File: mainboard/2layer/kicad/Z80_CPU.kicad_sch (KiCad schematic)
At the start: 62 parts, among them J2 C96ABC, J9 DIN-5, U71 CDB407, U72 CDB407, U73 CDB407, U74 CDB407, U90 Z80CPU

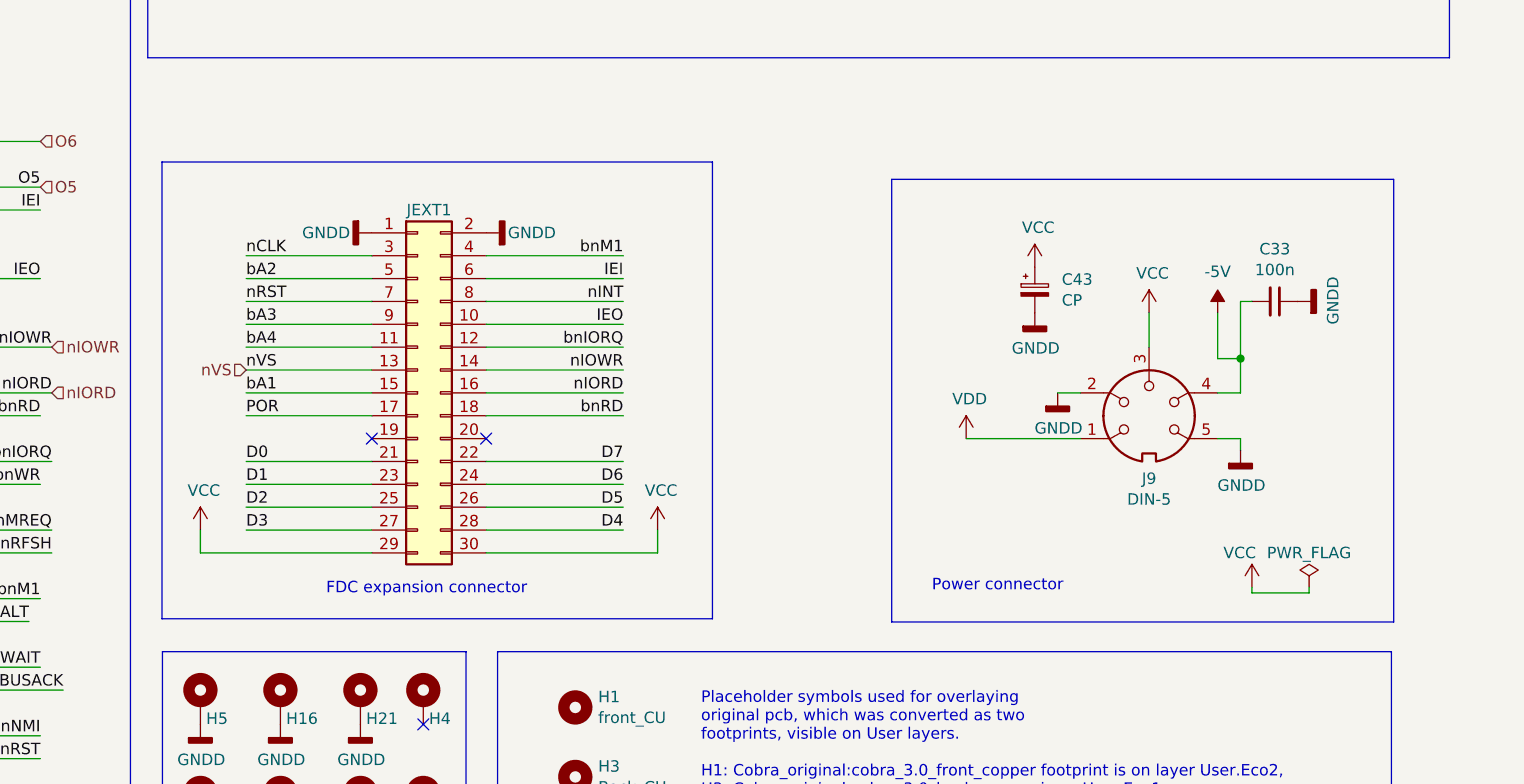
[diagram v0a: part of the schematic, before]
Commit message: Changed floppy connector, fixed some library paths
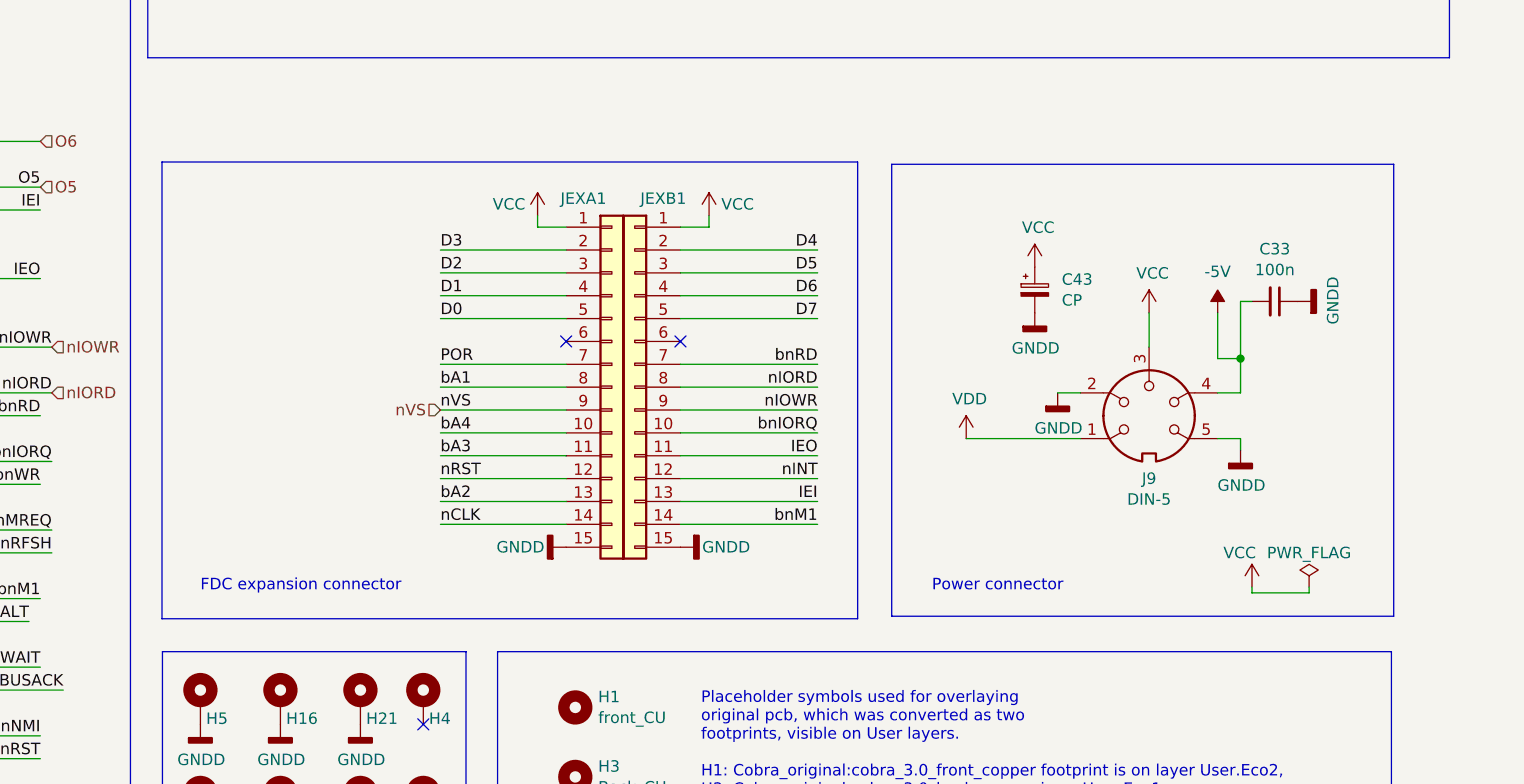
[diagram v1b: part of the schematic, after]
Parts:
- removed JEXT1: Conn_02x15_Odd_Even, Connector_PinHeader_2.54mm:PinHeader_2x15_P2.54mm_Vertical, symbol Connector_Generic:Conn_02x15_Odd_Even
- added JEXA1, JEXB1: Conn_01x15, Connector_PinHeader_2.54mm:PinHeader_1x15_P2.54mm_Vertical, symbol Connector_Generic:Conn_01x15
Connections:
- net D0: now also JEXA1.5 (Pin_5)
- net D1: now also JEXA1.4 (Pin_4)
- net D2: now also JEXA1.3 (Pin_3)
- net D3: now also JEXA1.2 (Pin_2)
- net D4: now also JEXB1.2 (Pin_2)
- net D5: now also JEXB1.3 (Pin_3)
- net D6: now also JEXB1.4 (Pin_4)
- net D7: now also JEXB1.5 (Pin_5)
- net GNDD: now also JEXA1.15 (Pin_15), JEXB1.15 (Pin_15)
- net IEI: now also JEXB1.13 (Pin_13)
- net IEO: now also JEXB1.11 (Pin_11)
- net POR: now also JEXA1.7 (Pin_7)
- net VCC: now also JEXA1.1 (Pin_1), JEXB1.1 (Pin_1)
- net bA1: now also JEXA1.8 (Pin_8)
- net bA2: now also JEXA1.13 (Pin_13)
- net bA3: now also JEXA1.11 (Pin_11)
- net bA4: now also JEXA1.10 (Pin_10)
- net bnIORQ: now also JEXB1.10 (Pin_10)
- net bnM1: now also JEXB1.14 (Pin_14)
- net bnRD: now also JEXB1.7 (Pin_7)
- net nCLK: now also JEXA1.14 (Pin_14)
- net nINT: now also JEXB1.12 (Pin_12)
- net nIORD: now also JEXB1.8 (Pin_8)
- net nIOWR: now also JEXB1.9 (Pin_9)
- net nRST: now also JEXA1.12 (Pin_12)
- net nVS: now also JEXA1.9 (Pin_9)

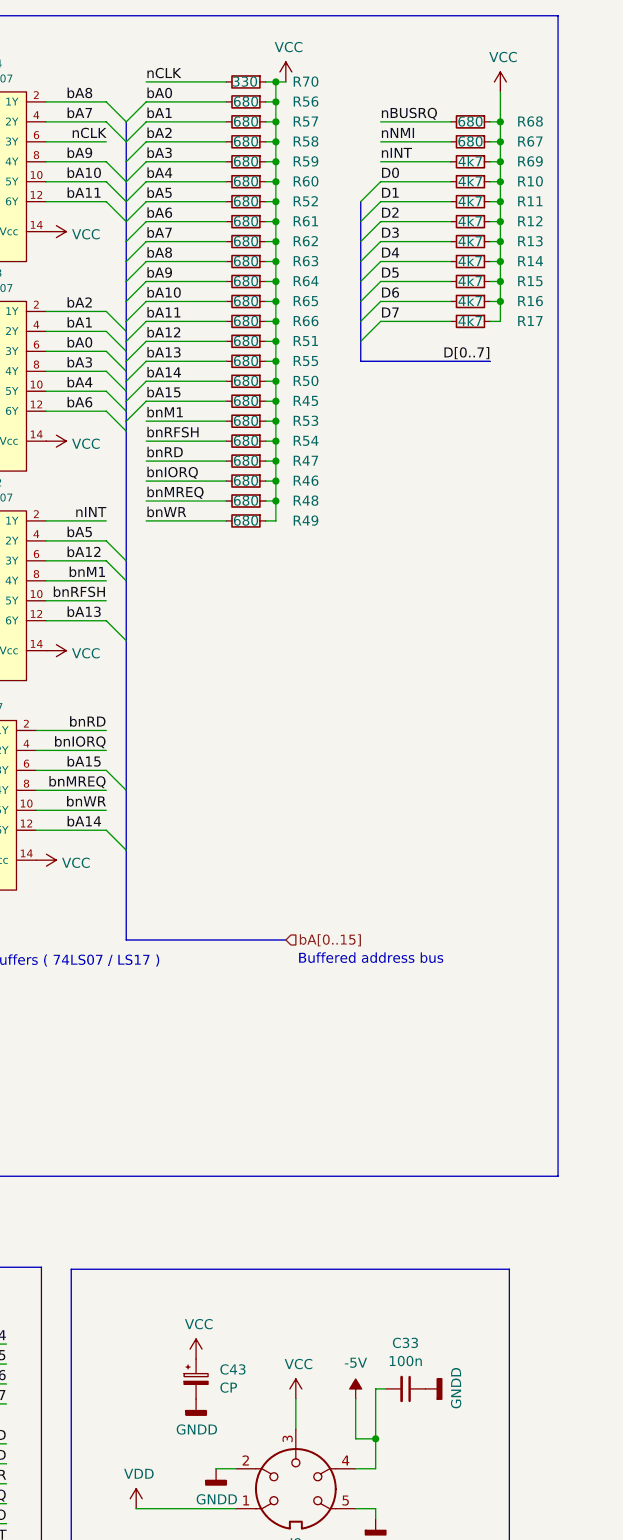
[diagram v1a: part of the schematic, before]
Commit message: Fixed some resistor values
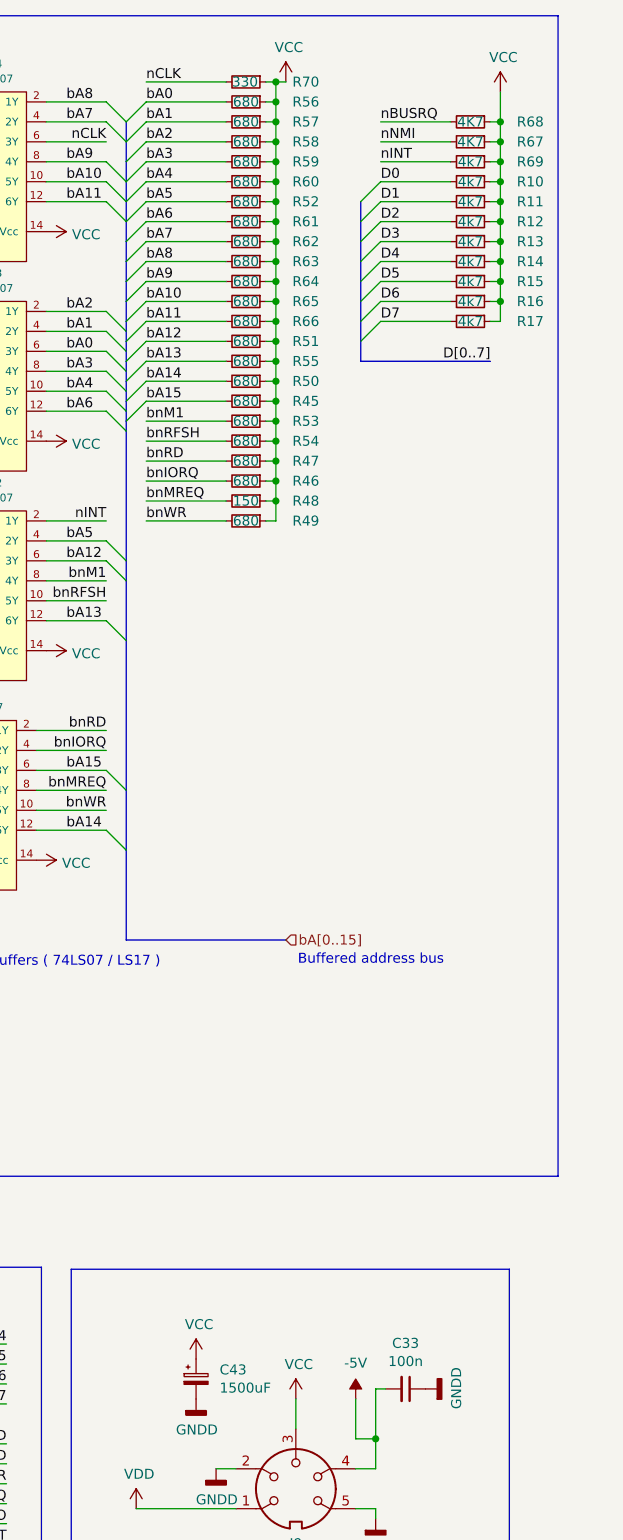
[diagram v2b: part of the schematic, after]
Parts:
- C43: value CP -> 1500uF
- R48: value 680 -> 150
- R67, R68: value 680 -> 4K7
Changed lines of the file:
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@@
       (effects (font (size 1.27 1.27)) (justify left))
     )
-    (property "Value" "CP" (at 154.1272 187.833 0)
+    (property "Value" "1500uF" (at 154.1272 187.833 0)
       (effects (font (size 1.27 1.27)) (justify left))
     )
@@
       (effects (font (size 1.27 1.27)))
     )
-    (property "Value" "680" (at 157.48 74.93 90)
+    (property "Value" "150" (at 157.48 74.93 90)
       (effects (font (size 1.27 1.27)))
     )
@@
       (effects (font (size 1.27 1.27)))
     )
-    (property "Value" "680" (at 186.055 26.67 90)
+    (property "Value" "4K7" (at 186.055 26.67 90)
       (effects (font (size 1.27 1.27)))
     )
@@
       (effects (font (size 1.27 1.27)))
     )
-    (property "Value" "680" (at 186.055 29.21 90)
-      (effects (font (size 1.27 1.27)))
-    )
+    (property "Value" "4K7" (at 186.055 29.21 90)
+      (effects (font (size 1.27 1.27)))
+    )

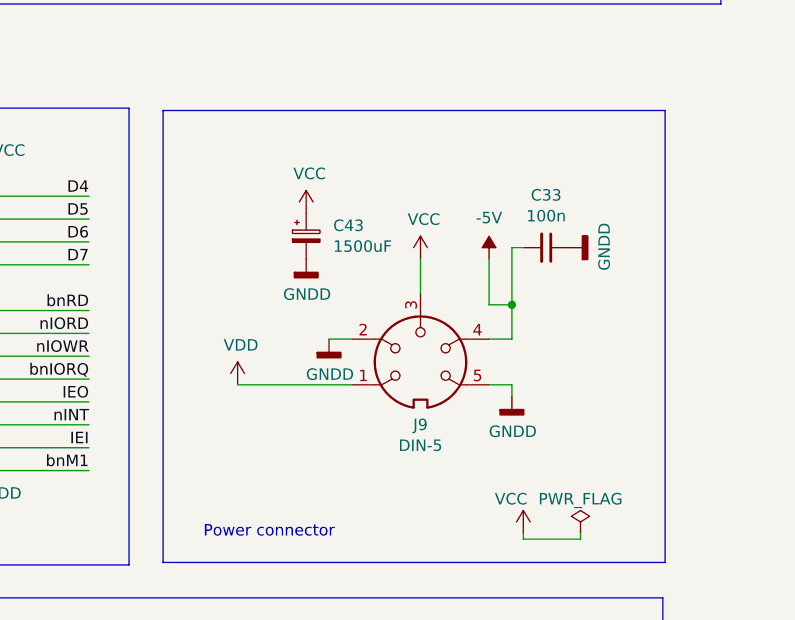
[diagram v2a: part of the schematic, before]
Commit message: Fixes for PCB DRC: trace clearance, footprints, board edges
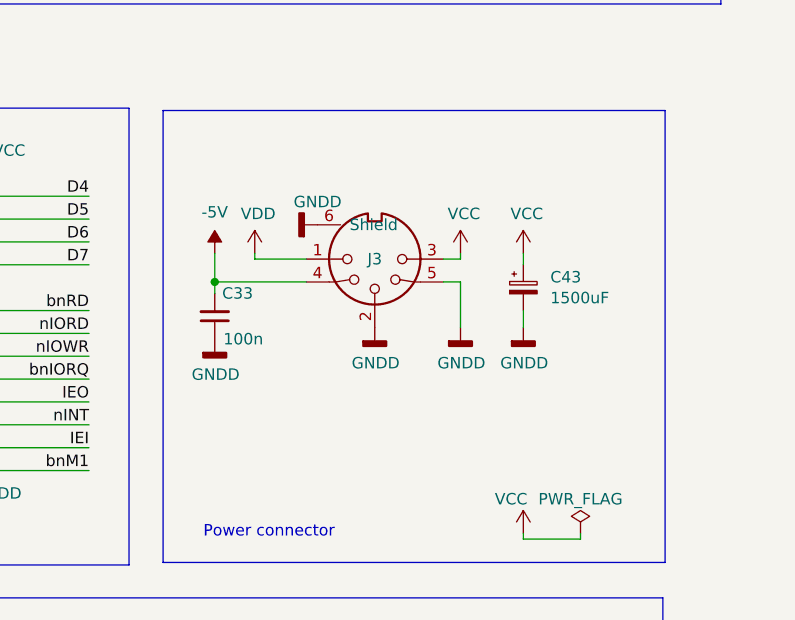
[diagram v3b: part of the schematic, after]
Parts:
- removed J9: DIN-5, Conectors_Unitra:DIN-5, symbol Connector:DIN-5
- added J3: DIN-5, Cobra_original:DIN-5, symbol Connector:DIN-5_180degree_GND
- C43: footprint Capacitor_THT:CP_Axial_L25.0mm_D10.0mm_P30.00mm_Horizontal -> Cobra_original:CP_Axial_L25.0mm_D9.0mm_P30.00mm_Horizontal
- H15, H16, H17, H18, H2, H21, H22, H23, H24, H25, H4, H5, H6, H7, H8: footprint MountingHole:MountingHole_2.5mm_Pad -> Cobra_original:MountingHole_2.5mm_Pad
- JEXA1, JEXB1: footprint Connector_PinHeader_2.54mm:PinHeader_1x15_P2.54mm_Vertical -> Cobra_original:PinHeader_1x15_P2.54mm_Vertical
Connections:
- net -5V: now also J3.4
- net GNDD: now also J3.2, J3.5, J3.6 (Shield)
- net VCC: now also J3.3
- net VDD: now also J3.1
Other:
- moved on the sheet: C43

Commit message: removed mounting holes and H1,H3 placeholders from the BOM/ibom, align C25 on PCB
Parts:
- H1, H3: now not fitted; now left out of the parts list
- H15, H16, H17, H18, H2, H21, H22, H23, H24, H25, H4, H5, H6, H7, H8: now left out of the parts list
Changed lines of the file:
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@@
   )
   (symbol (lib_id "Mechanical:MountingHole_Pad") (at 58.42 243.84 0) (unit 1)
-    (in_bom yes) (on_board yes) (dnp no)
+    (in_bom no) (on_board yes) (dnp no)
     (property "Reference" "H15" (at 59.055 245.745 0)
       (effects (font (size 1.27 1.27)) (justify left))
@@
   )
   (symbol (lib_id "Mechanical:MountingHole_Pad") (at 76.2 232.41 0) (unit 1)
-    (in_bom yes) (on_board yes) (dnp no)
+    (in_bom no) (on_board yes) (dnp no)
     (property "Reference" "H21" (at 76.835 234.315 0)
       (effects (font (size 1.27 1.27)) (justify left))
@@
   )
   (symbol (lib_id "Mechanical:MountingHole_Pad") (at 83.185 243.84 0) (unit 1)
-    (in_bom yes) (on_board yes) (dnp no)
+    (in_bom no) (on_board yes) (dnp no)
     (property "Reference" "H6" (at 83.82 245.745 0)
       (effects (font (size 1.27 1.27)) (justify left))
@@
   )
   (symbol (lib_id "Mechanical:MountingHole_Pad") (at 83.185 232.41 0) (unit 1)
-    (in_bom yes) (on_board yes) (dnp no)
+    (in_bom no) (on_board yes) (dnp no)
     (property "Reference" "H4" (at 83.82 234.315 0)
       (effects (font (size 1.27 1.27)) (justify left))
@@
   )
   (symbol (lib_id "Mechanical:MountingHole_Pad") (at 67.31 232.41 0) (unit 1)
-    (in_bom yes) (on_board yes) (dnp no)
+    (in_bom no) (on_board yes) (dnp no)
     (property "Reference" "H16" (at 67.945 234.315 0)
       (effects (font (size 1.27 1.27)) (justify left))
@@
   )
   (symbol (lib_id "Mechanical:MountingHole_Pad") (at 58.42 266.7 0) (unit 1)
-    (in_bom yes) (on_board yes) (dnp no)
+    (in_bom no) (on_board yes) (dnp no)
     (property "Reference" "H25" (at 59.055 268.605 0)
       (effects (font (size 1.27 1.27)) (justify left))
@@
   )
   (symbol (lib_id "Mechanical:MountingHole_Pad") (at 58.42 255.27 0) (unit 1)
-    (in_bom yes) (on_board yes) (dnp no)
+    (in_bom no) (on_board yes) (dnp no)
     (property "Reference" "H8" (at 59.055 257.175 0)
       (effects (font (size 1.27 1.27)) (justify left))
@@
   )
   (symbol (lib_id "Mechanical:MountingHole") (at 100.076 233.0704 0) (unit 1)
-    (in_bom yes) (on_board yes) (dnp no)
+    (in_bom no) (on_board yes) (dnp yes)
     (property "Reference" "H1" (at 102.616 231.902 0)
       (effects (font (size 1.27 1.27)) (justify left))
@@
       (effects (font (size 1.27 1.27)) hide)
     )
+    (property "Sim.Enable" "0" (at 100.076 233.0704 0)
+      (effects (font (size 1.27 1.27)) hide)
+    )
     (instances
       (project "main"
@@
   )
   (symbol (lib_id "Mechanical:MountingHole_Pad") (at 67.31 243.84 0) (unit 1)
-    (in_bom yes) (on_board yes) (dnp no)
+    (in_bom no) (on_board yes) (dnp no)
     (property "Reference" "H17" (at 67.945 245.745 0)
       (effects (font (size 1.27 1.27)) (justify left))
@@
   )
   (symbol (lib_id "Mechanical:MountingHole_Pad") (at 83.185 255.27 0) (unit 1)
-    (in_bom yes) (on_board yes) (dnp no)
+    (in_bom no) (on_board yes) (dnp no)
     (property "Reference" "H7" (at 83.82 257.175 0)
       (effects (font (size 1.27 1.27)) (justify left))
@@
   )
   (symbol (lib_id "Mechanical:MountingHole") (at 100.076 240.792 0) (unit 1)
-    (in_bom yes) (on_board yes) (dnp no)
+    (in_bom no) (on_board yes) (dnp yes)
     (property "Reference" "H3" (at 102.616 239.6236 0)
       (effects (font (size 1.27 1.27)) (justify left))
@@
       (effects (font (size 1.27 1.27)) hide)
     )
+    (property "Sim.Enable" "0" (at 100.076 240.792 0)
+      (effects (font (size 1.27 1.27)) hide)
+    )
     (instances
       (project "main"
@@
   )
   (symbol (lib_id "Mechanical:MountingHole_Pad") (at 76.2 266.7 0) (unit 1)
-    (in_bom yes) (on_board yes) (dnp no)
+    (in_bom no) (on_board yes) (dnp no)
     (property "Reference" "H24" (at 76.835 268.605 0)
       (effects (font (size 1.27 1.27)) (justify left))
@@
   )
   (symbol (lib_id "Mechanical:MountingHole_Pad") (at 76.2 243.84 0) (unit 1)
-    (in_bom yes) (on_board yes) (dnp no)
+    (in_bom no) (on_board yes) (dnp no)
     (property "Reference" "H22" (at 76.835 245.745 0)
       (effects (font (size 1.27 1.27)) (justify left))
@@
   )
   (symbol (lib_id "Mechanical:MountingHole_Pad") (at 76.2 255.27 0) (unit 1)
-    (in_bom yes) (on_board yes) (dnp no)
+    (in_bom no) (on_board yes) (dnp no)
     (property "Reference" "H23" (at 76.835 257.175 0)
       (effects (font (size 1.27 1.27)) (justify left))
@@
   )
   (symbol (lib_id "Mechanical:MountingHole_Pad") (at 67.31 266.7 0) (unit 1)
-    (in_bom yes) (on_board yes) (dnp no)
+    (in_bom no) (on_board yes) (dnp no)
     (property "Reference" "H2" (at 67.945 268.605 0)
       (effects (font (size 1.27 1.27)) (justify left))
@@
   )
   (symbol (lib_id "Mechanical:MountingHole_Pad") (at 58.42 232.41 0) (unit 1)
-    (in_bom yes) (on_board yes) (dnp no)
+    (in_bom no) (on_board yes) (dnp no)
     (property "Reference" "H5" (at 59.055 234.315 0)
       (effects (font (size 1.27 1.27)) (justify left))
@@
   )
   (symbol (lib_id "Mechanical:MountingHole_Pad") (at 67.31 255.27 0) (unit 1)
-    (in_bom yes) (on_board yes) (dnp no)
+    (in_bom no) (on_board yes) (dnp no)
     (property "Reference" "H18" (at 67.945 257.175 0)
       (effects (font (size 1.27 1.27)) (justify left))
